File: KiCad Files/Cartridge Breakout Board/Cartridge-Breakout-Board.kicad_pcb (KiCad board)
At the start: 2 copper layers, 68 x 25 mm, 8 parts

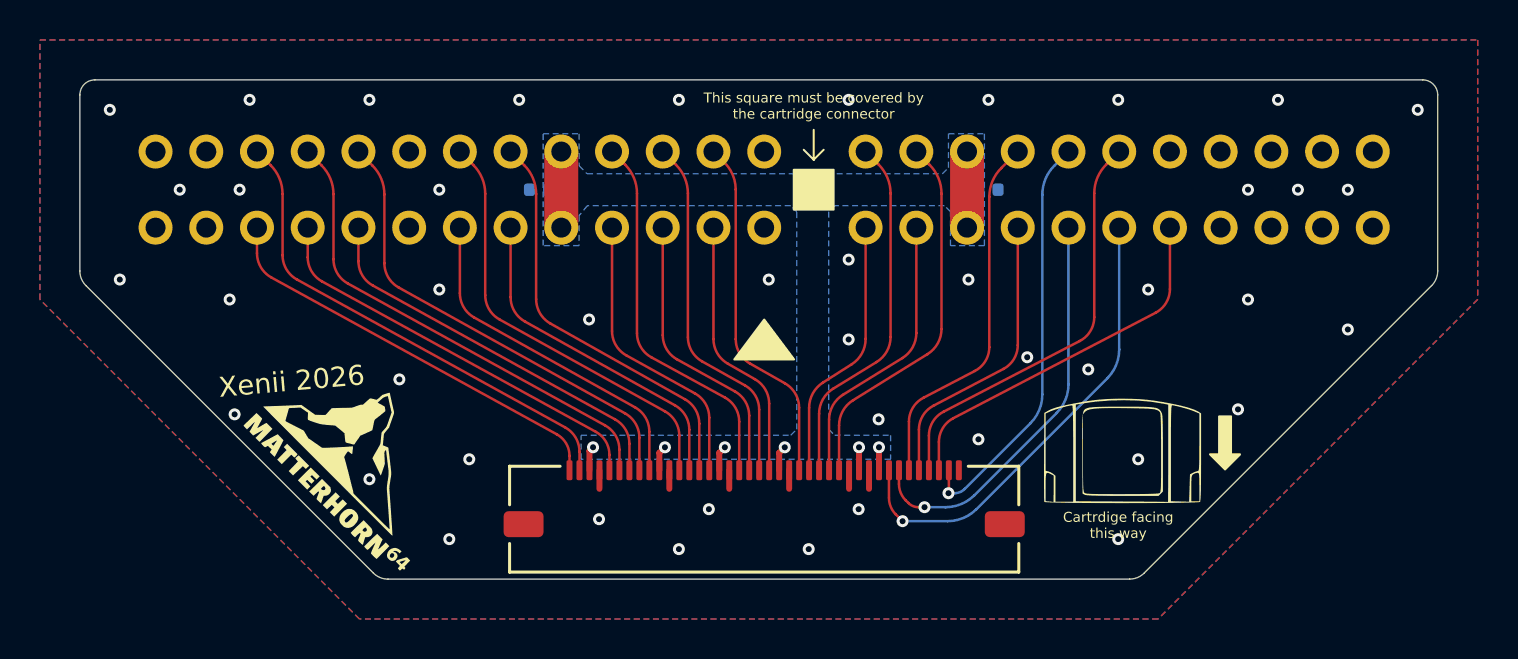
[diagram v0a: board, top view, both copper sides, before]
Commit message: Updated the cartridge breakout board to REV 1.1
Changes the cartridge connector which didn't have the correct pitch.
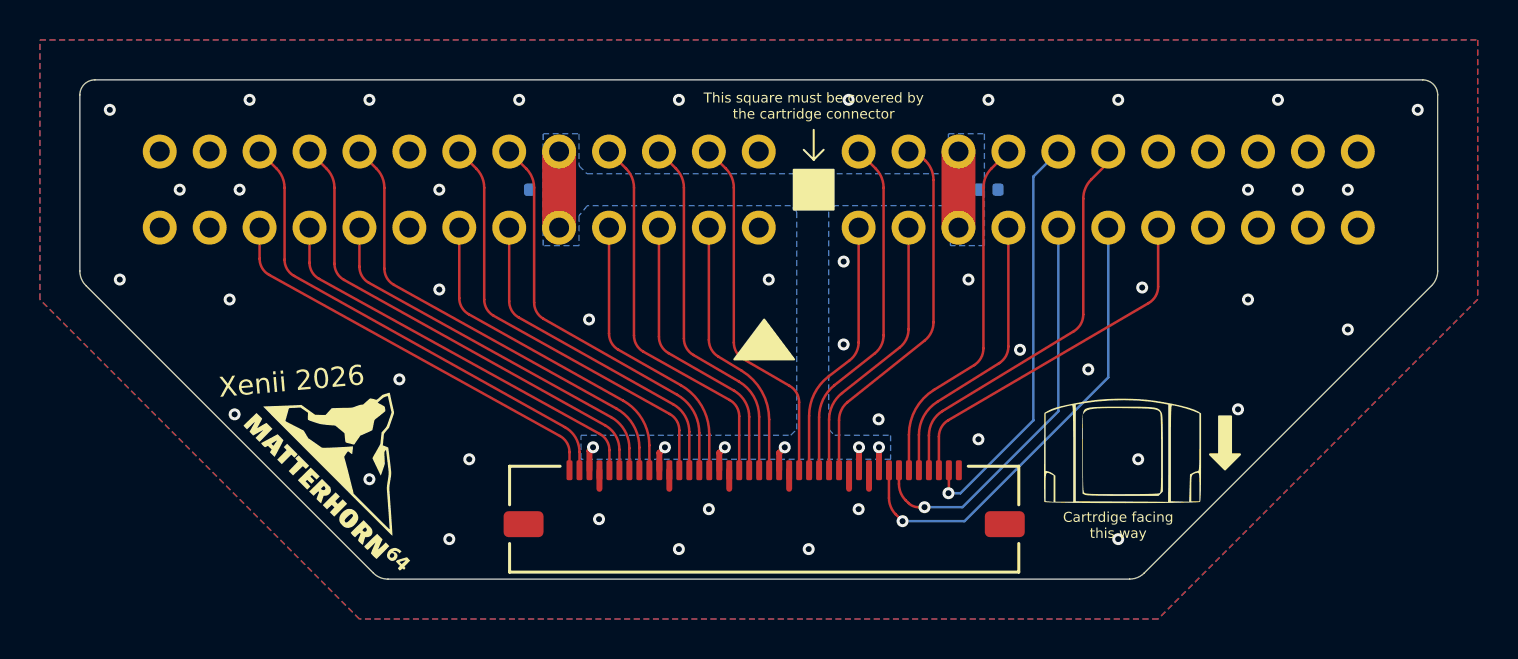
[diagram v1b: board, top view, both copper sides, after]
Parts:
- moved U1 2.27 mm to (119.0, 62.6)
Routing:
- net EXTJOY: track 18.9 -> 18.2 mm
- net /CAD7: track 18.9 -> 18.4 mm
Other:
- board text added: "MUS-002 | REV 1.1 | 29/6/2026 Matterhorn 64 CORE - Cartridge Breakout"
- board text removed: "MUS-002 | REV 1.0 | 14/5/2026 Matterhorn 64 CORE - Cartridge Breakout"
